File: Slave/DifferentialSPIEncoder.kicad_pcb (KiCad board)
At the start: 2 copper layers, 54 x 42.8 mm, 31 parts, among them J1 Debug, J2 8P8C_LED_Shielded, U2 AS5048A, U3 SN65HVD06D, U4 SN65HVD06D, U5 SN65HVD06D

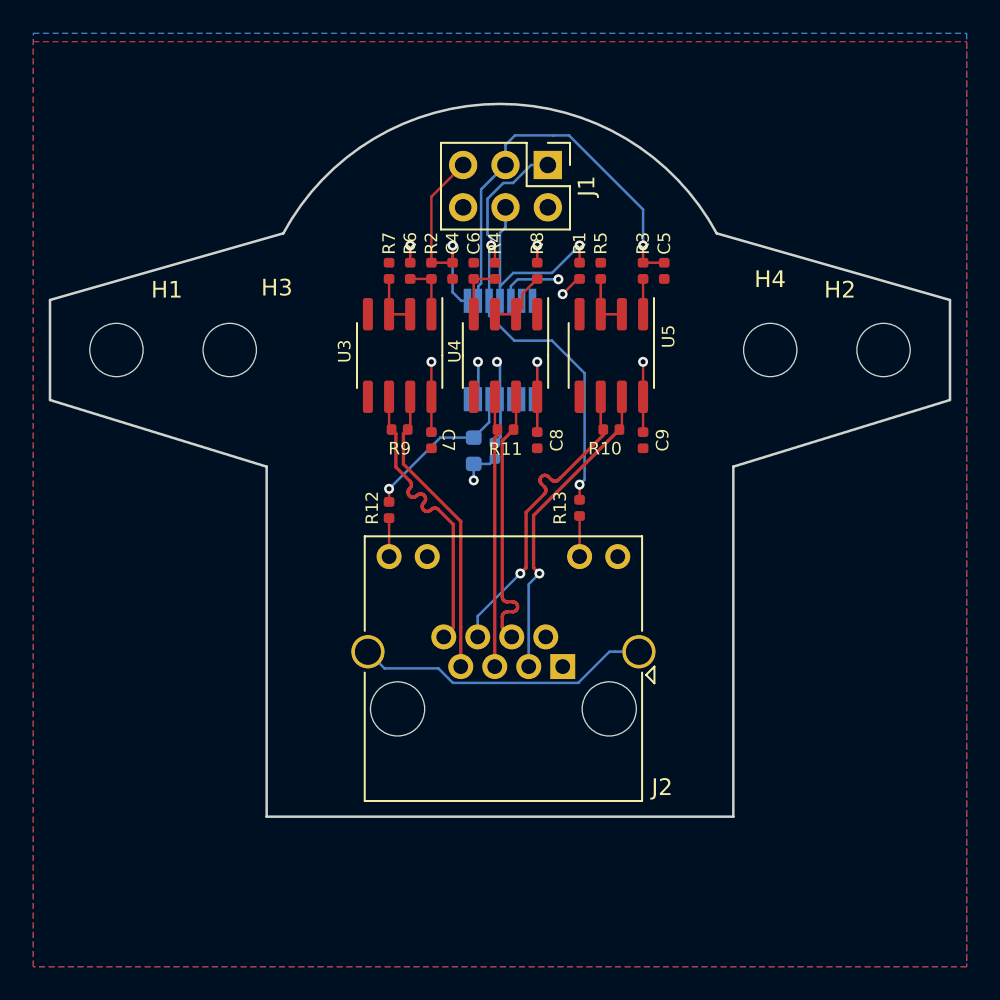
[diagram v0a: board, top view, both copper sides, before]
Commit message: Tweaks to layout to better fit AMT footprint
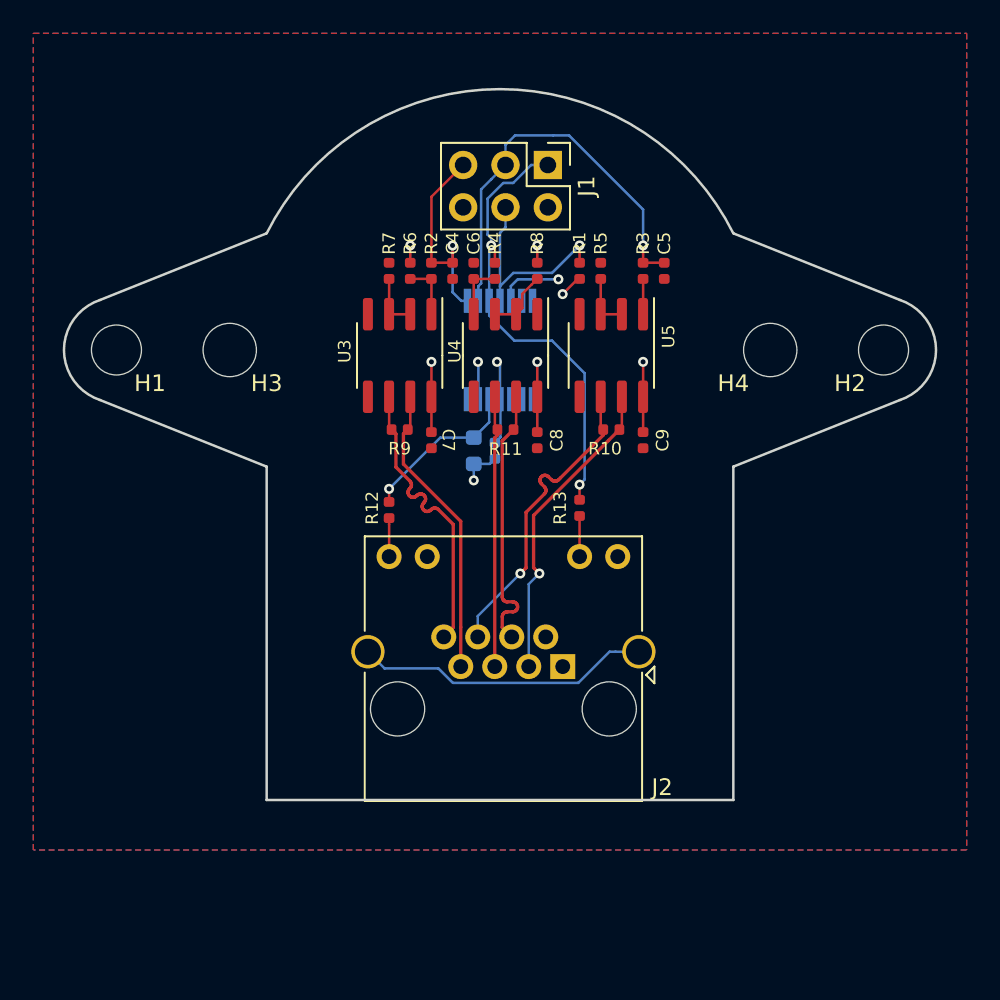
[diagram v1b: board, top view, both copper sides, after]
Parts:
- H1, H2: footprint MountingHole:MountingHole_3.2mm_M3 -> MountingHole:MountingHole_3mm
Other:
- board size 54 x 42.8 mm -> 52.3 x 42.7 mm
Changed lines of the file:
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@@
     (add_net ~CSn)
+  )
+  (module MountingHole:MountingHole_3mm (layer F.Cu)
+    (at 123.0125 100)
+    (descr "Mounting Hole 3mm, no annular")
+    (tags "mounting hole 3mm no annular")
+    (attr virtual)
+    (fp_text reference H2 (at -2.0125 2) (layer F.SilkS)
+      (effects (font (size 1 1) (thickness 0.15)))
+    )
+    (fp_text value MountingHole (at 0 4) (layer F.Fab)
+      (effects (font (size 1 1) (thickness 0.15)))
+    )
+    (fp_circle (center 0 0) (end 3.25 0) (layer F.CrtYd) (width 0.05))
+    (fp_circle (center 0 0) (end 3 0) (layer Cmts.User) (width 0.15))
+    (fp_text user %R (at 0.3 0) (layer F.Fab)
+      (effects (font (size 1 1) (thickness 0.15)))
+    )
+    (pad 1 np_thru_hole circle (at 0 0) (size 3 3) (drill 3) (layers *.Cu *.Mask))
+  )
+  (module MountingHole:MountingHole_3mm (layer F.Cu)
+    (at 76.9875 100)
+    (descr "Mounting Hole 3mm, no annular")
+    (tags "mounting hole 3mm no annular")
+    (attr virtual)
+    (fp_text reference H1 (at 2.0125 2) (layer F.SilkS)
+      (effects (font (size 1 1) (thickness 0.15)))
+    )
+    (fp_text value MountingHole (at 0 4) (layer F.Fab)
+      (effects (font (size 1 1) (thickness 0.15)))
+    )
+    (fp_circle (center 0 0) (end 3.25 0) (layer F.CrtYd) (width 0.05))
+    (fp_circle (center 0 0) (end 3 0) (layer Cmts.User) (width 0.15))
+    (fp_text user %R (at 0.3 0) (layer F.Fab)
+      (effects (font (size 1 1) (thickness 0.15)))
+    )
+    (pad 1 np_thru_hole circle (at 0 0) (size 3 3) (drill 3) (layers *.Cu *.Mask))
   )
   (module Connector_PinHeader_2.54mm:PinHeader_2x03_P2.54mm_Vertical (layer F.Cu)
@@
     (tags "mounting hole 3.2mm no annular m3")
     (attr virtual)
-    (fp_text reference H4 (at -0.01 -4.242) (layer F.SilkS)
+    (fp_text reference H4 (at -2.215 2) (layer F.SilkS)
       (effects (font (size 1 1) (thickness 0.15)))
     )
@@
     (tags "mounting hole 3.2mm no annular m3")
     (attr virtual)
-    (fp_text reference H3 (at 2.829 -3.734) (layer F.SilkS)
-      (effects (font (size 1 1) (thickness 0.15)))
-    )
-    (fp_text value MountingHole (at 0 4.2) (layer F.Fab)
-      (effects (font (size 1 1) (thickness 0.15)))
-    )
-    (fp_text user %R (at 0.3 0) (layer F.Fab)
-      (effects (font (size 1 1) (thickness 0.15)))
-    )
-    (fp_circle (center 0 0) (end 3.2 0) (layer Cmts.User) (width 0.15))
-    (fp_circle (center 0 0) (end 3.45 0) (layer F.CrtYd) (width 0.05))
-    (pad 1 np_thru_hole circle (at 0 0) (size 3.2 3.2) (drill 3.2) (layers *.Cu *.Mask))
-  )
-  (module MountingHole:MountingHole_3.2mm_M3 (layer F.Cu)
-    (at 123.0125 100)
-    (descr "Mounting Hole 3.2mm, no annular, M3")
-    (tags "mounting hole 3.2mm no annular m3")
-    (attr virtual)
-    (fp_text reference H2 (at -2.6165 -3.607) (layer F.SilkS)
-      (effects (font (size 1 1) (thickness 0.15)))
-    )
-    (fp_text value MountingHole (at 0 4.2) (layer F.Fab)
-      (effects (font (size 1 1) (thickness 0.15)))
-    )
-    (fp_text user %R (at 0.3 0) (layer F.Fab)
-      (effects (font (size 1 1) (thickness 0.15)))
-    )
-    (fp_circle (center 0 0) (end 3.2 0) (layer Cmts.User) (width 0.15))
-    (fp_circle (center 0 0) (end 3.45 0) (layer F.CrtYd) (width 0.05))
-    (pad 1 np_thru_hole circle (at 0 0) (size 3.2 3.2) (drill 3.2) (layers *.Cu *.Mask))
-  )
-  (module MountingHole:MountingHole_3.2mm_M3 (layer F.Cu)
-    (at 76.9875 100)
-    (descr "Mounting Hole 3.2mm, no annular, M3")
-    (tags "mounting hole 3.2mm no annular m3")
-    (attr virtual)
-    (fp_text reference H1 (at 3.0225 -3.607) (layer F.SilkS)
+    (fp_text reference H3 (at 2.215 2) (layer F.SilkS)
       (effects (font (size 1 1) (thickness 0.15)))
     )
@@
     )
   )
-  (gr_arc (start 100 100) (end 112.999998 93.000001) (angle -123.3984866) (layer Edge.Cuts) (width 0.15))
-  (gr_line (start 114 107) (end 114 128) (layer Edge.Cuts) (width 0.15))
-  (gr_line (start 127 103) (end 114 107) (layer Edge.Cuts) (width 0.15))
-  (gr_line (start 127 97) (end 127 103) (layer Edge.Cuts) (width 0.15))
-  (gr_line (start 112.999999 93) (end 127 97) (layer Edge.Cuts) (width 0.15))
-  (gr_line (start 73 97) (end 87 93) (layer Edge.Cuts) (width 0.15))
-  (gr_line (start 73 103) (end 73 97) (layer Edge.Cuts) (width 0.15))
-  (gr_line (start 86 107) (end 73 103) (layer Edge.Cuts) (width 0.15))
-  (gr_line (start 86 128) (end 86 107) (layer Edge.Cuts) (width 0.15))
-  (gr_line (start 86 128) (end 114 128) (layer Edge.Cuts) (width 0.15))
+  (gr_arc (start 123 100) (end 123.999999 102.999999) (angle -143.1301024) (layer Edge.Cuts) (width 0.15))
+  (gr_arc (start 77 100) (end 76.000001 97.000001) (angle -143.1301024) (layer Edge.Cuts) (width 0.15))
+  (gr_arc (start 100 100) (end 113.999999 93.000001) (angle -126.869896) (layer Edge.Cuts) (width 0.15))
+  (gr_line (start 114 107) (end 114 127) (layer Edge.Cuts) (width 0.15))
+  (gr_line (start 123.999999 103) (end 114 107) (layer Edge.Cuts) (width 0.15))
+  (gr_line (start 114 93) (end 124 97) (layer Edge.Cuts) (width 0.15))
+  (gr_line (start 76.000001 97.000001) (end 86.000001 93) (layer Edge.Cuts) (width 0.15))
+  (gr_line (start 86 107) (end 76 102.999999) (layer Edge.Cuts) (width 0.15))
+  (gr_line (start 86 127) (end 86 107) (layer Edge.Cuts) (width 0.15))
+  (gr_line (start 86 127) (end 114 127) (layer Edge.Cuts) (width 0.15))
   (gr_circle (center 100 100) (end 123.0125 100) (layer Dwgs.User) (width 0.15))
   (gr_circle (center 100 100) (end 116.215 100) (layer Dwgs.User) (width 0.15))
@@
     (polygon
       (pts
-        (xy 72 81.5) (xy 128 81.5) (xy 128 137) (xy 72 137)
+        (xy 72 81) (xy 128 81) (xy 128 130) (xy 72 130)
       )
     )
@@
     (polygon
       (pts
-        (xy 72 81) (xy 128 81) (xy 128 137) (xy 72 137)
+        (xy 72 81) (xy 128 81) (xy 128 130) (xy 72 130)
       )
     )

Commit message: Add silkscreen with info
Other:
- board text added: "AS5048A Encoder Rev 2 2019-12-02"
- board text added: "https://github.com/Wetmelon/DifferentialSPIEncoder"
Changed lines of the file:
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@@
   (general
     (thickness 1.6)
-    (drawings 12)
+    (drawings 14)
     (tracks 282)
     (zones 0)
@@
     (tags "SSOP 0.65")
     (attr smd)
-    (fp_text reference U2 (at 0 3.607 270) (layer B.SilkS)
+    (fp_text reference U2 (at -1 3.607 270) (layer B.SilkS)
       (effects (font (size 1 1) (thickness 0.15)) (justify mirror))
     )
@@
     )
   )
+  (gr_text "AS5048A Encoder\nRev 2\n2019-12-02" (at 111 100 90) (layer B.SilkS)
+    (effects (font (size 0.75 0.75) (thickness 0.1)) (justify mirror))
+  )
+  (gr_text https://github.com/Wetmelon/DifferentialSPIEncoder (at 100 125) (layer B.SilkS)
+    (effects (font (size 0.65 0.65) (thickness 0.1)) (justify mirror))
+  )
   (gr_arc (start 123 100) (end 123.999999 102.999999) (angle -143.1301024) (layer Edge.Cuts) (width 0.15))
